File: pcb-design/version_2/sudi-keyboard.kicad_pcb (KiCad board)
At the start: 2 copper layers, 123.4 x 99.4 mm, 169 parts, among them J1 SIDE_CON, J2 SWD_JLINK, J3 0.91 OLED, J4 BatCon, J5 SIDE_CON, K1 KEYSW, K10 KEYSW, K11 KEYSW, K12 KEYSW, K13 KEYSW, K14 KEYSW, K15 KEYSW, K16 KEYSW, K17 KEYSW, K18 KEYSW, K2 KEYSW, K3 KEYSW, K4 KEYSW, K5 KEYSW, K6 KEYSW, K7 KEYSW, K8 KEYSW, K9 KEYSW, P1 USB_C_Plug_USB2.0, Q1 PJA3404_(G1,D3,S2), Q2 PJA3405_(G1,D3,S2), SW1 RST, SW3 PWR_SWITCH, SW4 5V_EN, U10 MAX17048, U4 CH340C, U5 BQ24075RGT_DPPM, U6 TPS63002_SEPIC_5V, U7 nRF52832-QFxx, U8 MCP23017_SS, U9 TPS63001_SEPIC_3V3, Y1 32MHz_CF4032M00020001

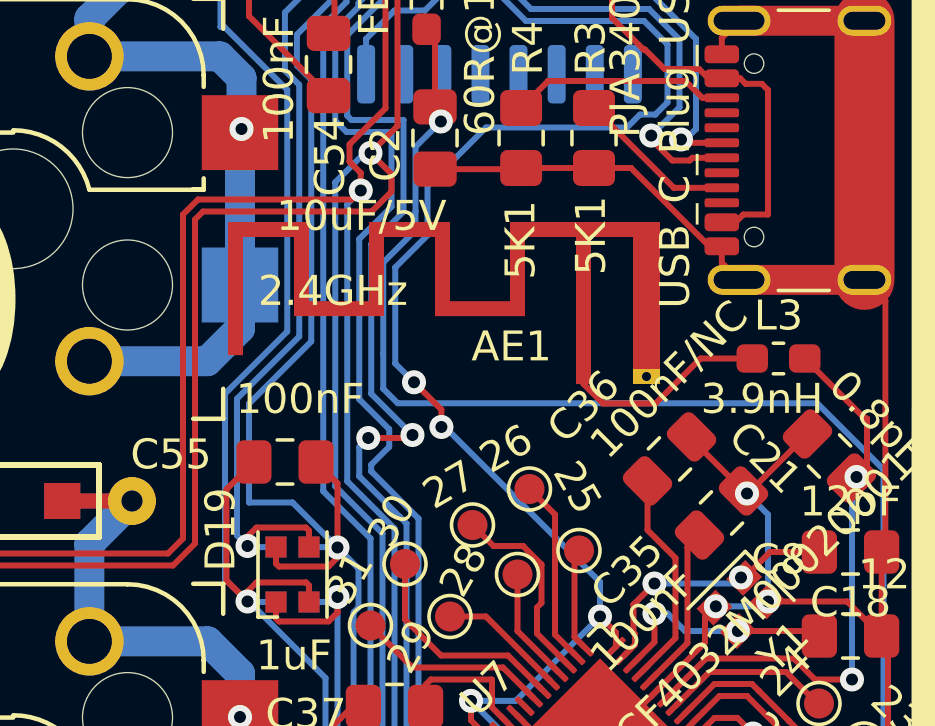
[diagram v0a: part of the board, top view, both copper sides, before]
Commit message: [12-16-2150] add capacitor to anntena
renamed kicad project
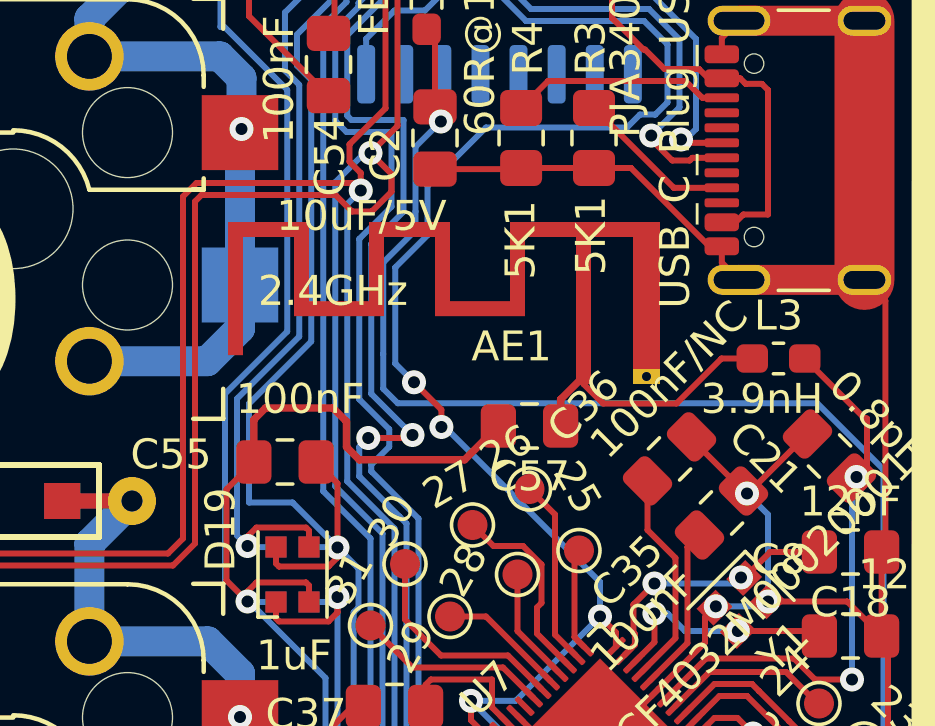
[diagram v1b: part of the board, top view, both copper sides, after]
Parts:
- added C57: 1.5pF, Capacitor_SMD:C_0805_2012Metric_Pad1.18x1.45mm_HandSolder, F.Cu at (218.1, 90.3)
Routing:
- net GND: track 787.6 -> 799.0 mm
- net Net-(AE1-A): track 6.77 -> 8.73 mm
- net SDA: track 173.1 -> 173.9 mm
- net SCL: track 159.0 -> 159.6 mm

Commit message: [01-19-2213] generate gerber and order pcb
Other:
- board text removed: "MAKE Front Back MCP23017 MAKE Front Back RJ12 Socket"
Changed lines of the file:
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@@
 		(allow_soldermask_bridges_in_footprints no)
 		(pcbplotparams
-			(layerselection 0x0000000_7fffffff)
-			(plot_on_all_layers_selection 0x004bf02_00000000)
+			(layerselection 0x7ffffff_ffffffff)
+			(plot_on_all_layers_selection 0x0000000_00000000)
 			(disableapertmacros no)
 			(usegerberextensions no)
@@
 			(sketchpadsonfab no)
 			(subtractmaskfromsilk no)
-			(outputformat 4)
+			(outputformat 1)
 			(mirror no)
-			(drillshape 1)
+			(drillshape 0)
 			(scaleselection 1)
-			(outputdirectory "output/")
+			(outputdirectory "output/gerber/")
 		)
 	)
@@
 		)
 	)
-	(gr_text "MAKE Front Back MCP23017\nMAKE Front Back RJ12 Socket"
-		(at 257.735 -143.67522 0)
-		(layer "User.1")
-		(effects
-			(font
-				(size 5 5)
-				(thickness 1.25)
-				(bold yes)
-			)
-			(justify left bottom)
-		)
-	)

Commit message: [02-08-1952] Ordering Component From LCSC
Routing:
- net +BATT: track 70.6 -> 69.2 mm
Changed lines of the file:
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@@
 	)
 	(segment
-		(start 179.399999 130.849999)
-		(end 178.2 129.65)
-		(width 0.2)
-		(layer "F.Cu")
-		(net 58)
-	)
-	(segment
-		(start 171.660051 112.9)
-		(end 171.060051 112.3)
+		(start 173.23995 111.9)
+		(end 172.23995 112.9)
 		(width 0.2)
 		(layer "F.Cu")
@@
 	)
 	(segment
-		(start 179.399999 131.949998)
-		(end 179.399999 130.849999)
+		(start 142.449999 122.159997)
+		(end 144.059996 120.55)
 		(width 0.2)
 		(layer "F.Cu")
@@
 	)
 	(segment
-		(start 142.449999 122.159997)
-		(end 144.059996 120.55)
+		(start 171.060051 112.3)
+		(end 165.494744 112.3)
+		(width 0.2)
+		(layer "F.Cu")
+		(net 58)
+	)
+	(segment
+		(start 172.23995 112.9)
+		(end 171.660051 112.9)
 		(width 0.2)
 		(layer "F.Cu")
@@
 	)
 	(segment
-		(start 161.634744 116.16)
-		(end 158.279058 116.16)
+		(start 173.225 127.325)
+		(end 173.225 115.075)
 		(width 0.2)
 		(layer "F.Cu")
@@
 	)
 	(segment
-		(start 178.2 129.65)
-		(end 174.15 129.65)
-		(width 0.2)
-		(layer "F.Cu")
-		(net 58)
-	)
-	(segment
-		(start 171.060051 112.3)
-		(end 165.494744 112.3)
-		(width 0.2)
-		(layer "F.Cu")
-		(net 58)
-	)
-	(segment
-		(start 173.225 115.075)
-		(end 174.25 114.05)
+		(start 161.634744 116.16)
+		(end 158.279058 116.16)
 		(width 0.2)
 		(layer "F.Cu")
@@
 	)
 	(segment
-		(start 174.85 128.95)
+		(start 171.660051 112.9)
+		(end 171.060051 112.3)
+		(width 0.2)
+		(layer "F.Cu")
+		(net 58)
+	)
+	(segment
+		(start 179.399999 131.949998)
+		(end 179.399999 130.849999)
+		(width 0.2)
+		(layer "F.Cu")
+		(net 58)
+	)
+	(segment
+		(start 175.55 129.65)
 		(end 173.225 127.325)
 		(width 0.2)
@@
 	)
 	(segment
-		(start 173.23995 111.9)
-		(end 172.23995 112.9)
+		(start 155.519058 113.4)
+		(end 154.4875 113.4)
+		(width 0.2)
+		(layer "F.Cu")
+		(net 58)
+	)
+	(segment
+		(start 179.399999 130.849999)
+		(end 178.2 129.65)
 		(width 0.2)
 		(layer "F.Cu")
@@
 	)
 	(segment
-		(start 173.225 127.325)
-		(end 173.225 115.075)
-		(width 0.2)
-		(layer "F.Cu")
-		(net 58)
-	)
-	(segment
-		(start 174.15 129.65)
-		(end 174.85 128.95)
-		(width 0.2)
-		(layer "F.Cu")
-		(net 58)
-	)
-	(segment
-		(start 172.23995 112.9)
-		(end 171.660051 112.9)
+		(start 178.2 129.65)
+		(end 175.55 129.65)
 		(width 0.2)
 		(layer "F.Cu")
@@
 		(start 174.25 114.05)
 		(end 174.25 112.215686)
-		(width 0.2)
-		(layer "F.Cu")
-		(net 58)
-	)
-	(segment
-		(start 155.519058 113.4)
-		(end 154.4875 113.4)
 		(width 0.2)
 		(layer "F.Cu")
@@
 		(width 0.2)
 		(layer "F.Cu")
+		(net 58)
+	)
+	(segment
+		(start 173.225 115.075)
+		(end 174.25 114.05)
+		(width 0.2)
+		(layer "F.Cu")
